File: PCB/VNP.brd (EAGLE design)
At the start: 24.8 x 106.7 mm, 10 parts, among them U1 VR

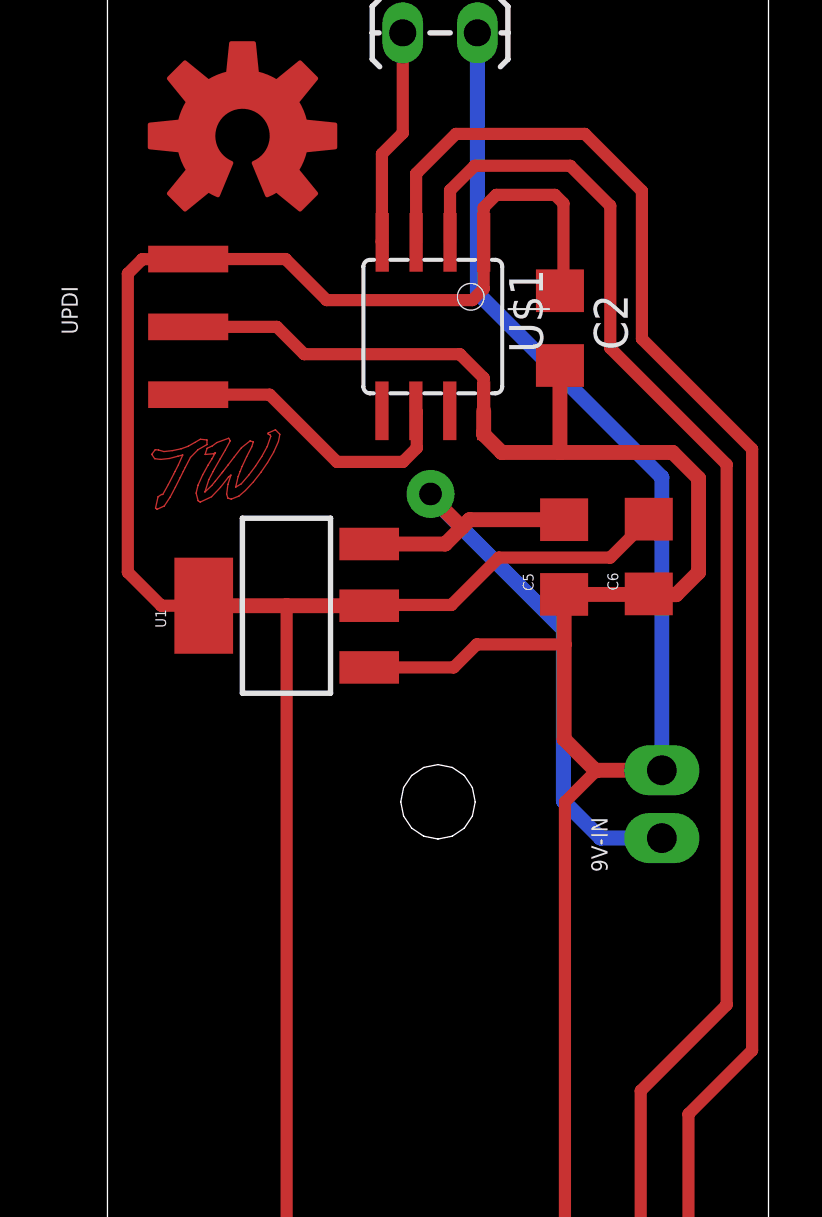
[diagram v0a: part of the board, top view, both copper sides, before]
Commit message: PCB Logo Updates
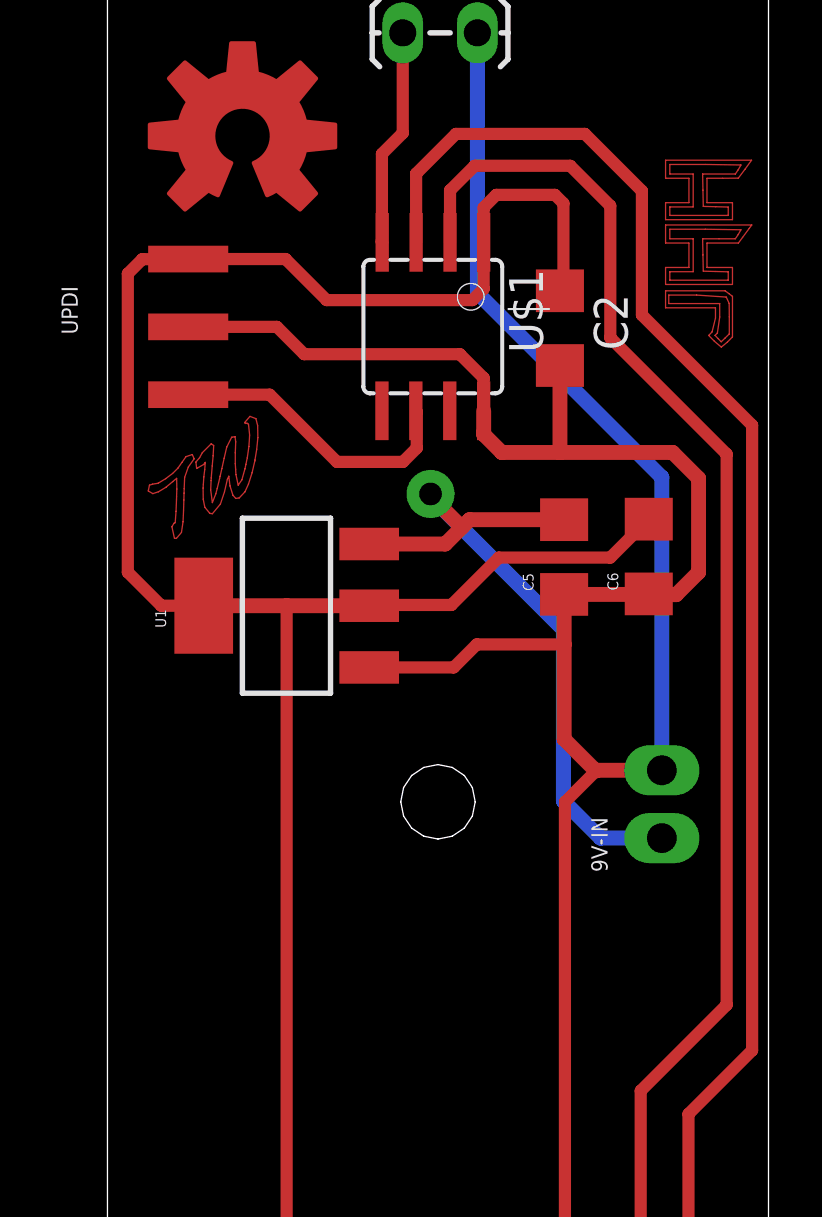
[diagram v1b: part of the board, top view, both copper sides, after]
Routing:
- net N$16: track 0.00 -> 14.2 mm
- net N$18: track 0.00 -> 14.2 mm
- net N$17: track 0.00 -> 12.6 mm
- net N$19: track 0.00 -> 12.6 mm
- net N$14: track 0.00 -> 8.91 mm
- net N$15: track 0.00 -> 7.78 mm
